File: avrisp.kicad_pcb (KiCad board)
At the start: 2 copper layers, 25 parts, among them J3 USB_A, J4 CONN_02X05, U1 ATMEGA8-16PU, Y1 12MHz

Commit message: last changes
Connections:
- net Net-(D3-Pad3) renamed /data+
- net Net-(D4-Pad3) renamed /data-
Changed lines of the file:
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@@
   (layers
     (0 F.Cu signal)
-    (31 B.Cu signal hide)
-    (32 B.Adhes user hide)
-    (33 F.Adhes user hide)
-    (34 B.Paste user hide)
-    (35 F.Paste user hide)
-    (36 B.SilkS user hide)
-    (37 F.SilkS user hide)
-    (38 B.Mask user hide)
-    (39 F.Mask user hide)
-    (40 Dwgs.User user hide)
-    (41 Cmts.User user hide)
-    (42 Eco1.User user hide)
-    (43 Eco2.User user hide)
-    (44 Edge.Cuts user hide)
-    (45 Margin user hide)
-    (46 B.CrtYd user hide)
-    (47 F.CrtYd user hide)
-    (48 B.Fab user hide)
-    (49 F.Fab user hide)
+    (31 B.Cu signal)
+    (32 B.Adhes user)
+    (33 F.Adhes user)
+    (34 B.Paste user)
+    (35 F.Paste user)
+    (36 B.SilkS user)
+    (37 F.SilkS user)
+    (38 B.Mask user)
+    (39 F.Mask user)
+    (40 Dwgs.User user)
+    (41 Cmts.User user)
+    (42 Eco1.User user)
+    (43 Eco2.User user)
+    (44 Edge.Cuts user)
+    (45 Margin user)
+    (46 B.CrtYd user)
+    (47 F.CrtYd user)
+    (48 B.Fab user)
+    (49 F.Fab user)
   )
   (setup
@@
   (net 32 "Net-(J4-Pad2)")
   (net 33 "Net-(J4-Pad3)")
-  (net 34 "Net-(D4-Pad3)")
-  (net 35 "Net-(D3-Pad3)")
+  (net 34 /data-)
+  (net 35 /data+)
   (net_class Default "This is the default net class."
     (clearance 0.7)
@@
     (diff_pair_width 0.2)
     (add_net +5V)
+    (add_net /data+)
+    (add_net /data-)
     (add_net GND)
     (add_net "Net-(C1-Pad1)")
@@
     (add_net "Net-(D2-Pad1)")
     (add_net "Net-(D2-Pad2)")
-    (add_net "Net-(D3-Pad3)")
-    (add_net "Net-(D4-Pad3)")
     (add_net "Net-(J4-Pad1)")
     (add_net "Net-(J4-Pad2)")
@@
       (net 7 +5V))
     (pad 2 thru_hole circle (at 2.54 0 180) (size 1.5 1.5) (drill 0.9) (layers *.Cu *.Mask)
-      (net 34 "Net-(D4-Pad3)"))
+      (net 34 /data-))
     (pad 3 thru_hole circle (at 4.57 0 180) (size 1.5 1.5) (drill 0.9) (layers *.Cu *.Mask)
-      (net 35 "Net-(D3-Pad3)"))
+      (net 35 /data+))
     (pad 4 thru_hole circle (at 7.11 0 180) (size 1.5 1.5) (drill 0.9) (layers *.Cu *.Mask)
       (net 1 GND))
@@
       (net 7 +5V))
     (pad 2 thru_hole oval (at 10.16 0 180) (size 1.6 1.6) (drill 0.8) (layers *.Cu *.Mask)
-      (net 34 "Net-(D4-Pad3)"))
+      (net 34 /data-))
     (model Resistors_THT.3dshapes/R_Axial_DIN0207_L6.3mm_D2.5mm_P10.16mm_Horizontal.wrl
       (at (xyz 0 0 0))
@@
     (fp_line (start 1.93 -1.25) (end 1.93 1.25) (layer F.Fab) (width 0.1))
     (pad 2 thru_hole oval (at 10.16 0 180) (size 1.6 1.6) (drill 0.8) (layers *.Cu *.Mask)
-      (net 34 "Net-(D4-Pad3)"))
+      (net 34 /data-))
     (pad 1 thru_hole circle (at 0 0 180) (size 1.6 1.6) (drill 0.8) (layers *.Cu *.Mask)
       (net 15 "Net-(R8-Pad1)"))
@@
     (fp_line (start 1.93 -1.25) (end 1.93 1.25) (layer F.Fab) (width 0.1))
     (pad 2 thru_hole oval (at 10.16 0) (size 1.6 1.6) (drill 0.8) (layers *.Cu *.Mask)
-      (net 35 "Net-(D3-Pad3)"))
+      (net 35 /data+))
     (pad 1 thru_hole circle (at 0 0) (size 2 2) (drill 0.8) (layers *.Cu *.Mask)
       (net 2 "Net-(R9-Pad1)"))
@@
     (pad 2 smd rect (at -1 0.95) (size 0.9 0.8) (layers F.Cu F.Paste F.Mask))
     (pad 3 smd rect (at 1 0) (size 0.9 0.8) (layers F.Cu F.Paste F.Mask)
-      (net 35 "Net-(D3-Pad3)"))
+      (net 35 /data+))
     (model ${KISYS3DMOD}/TO_SOT_Packages_SMD.3dshapes/SOT-23.wrl
       (at (xyz 0 0 0))
@@
     )
     (pad 3 smd rect (at 1 0) (size 0.9 0.8) (layers F.Cu F.Paste F.Mask)
-      (net 34 "Net-(D4-Pad3)"))
+      (net 34 /data-))
     (pad 2 smd rect (at -1 0.95) (size 0.9 0.8) (layers F.Cu F.Paste F.Mask))
     (pad 1 smd rect (at -1 -0.95) (size 0.9 0.8) (layers F.Cu F.Paste F.Mask)

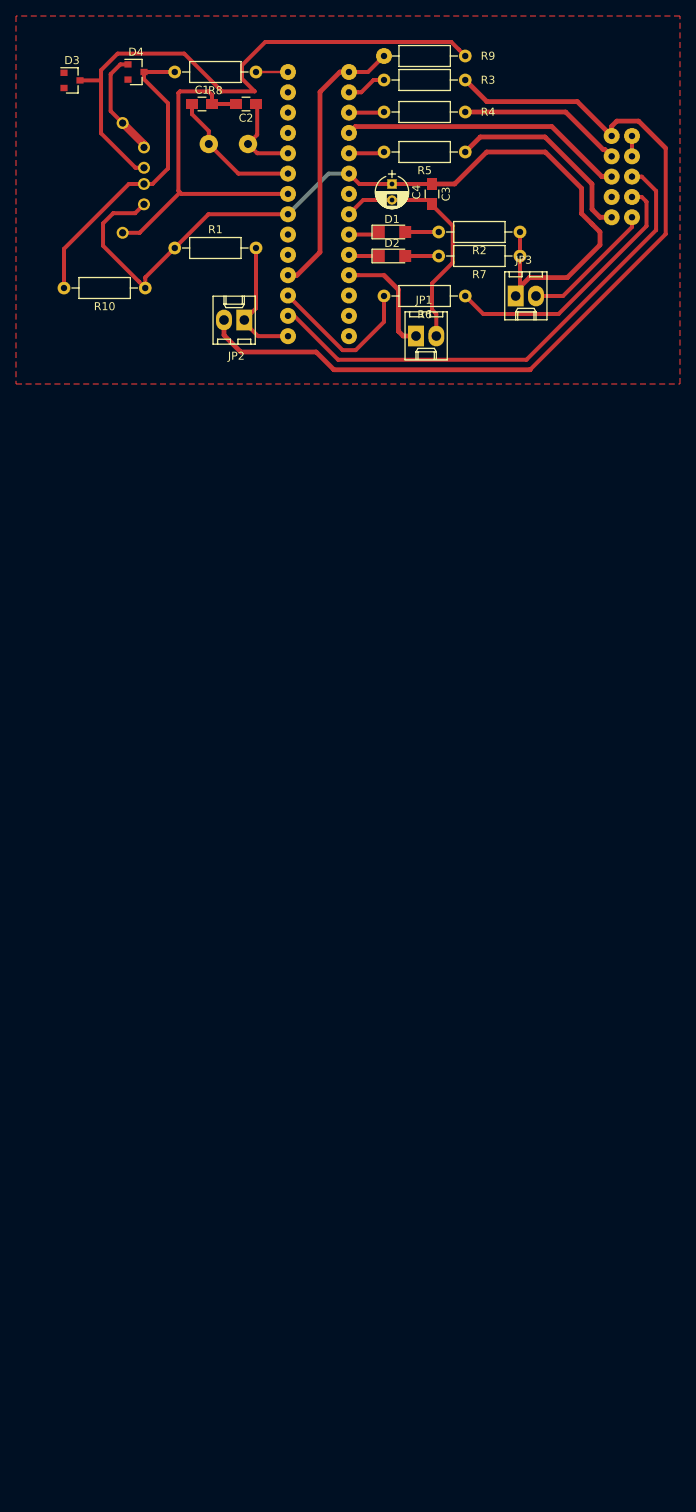
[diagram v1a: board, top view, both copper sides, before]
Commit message: Make one sided PCB but with smd components
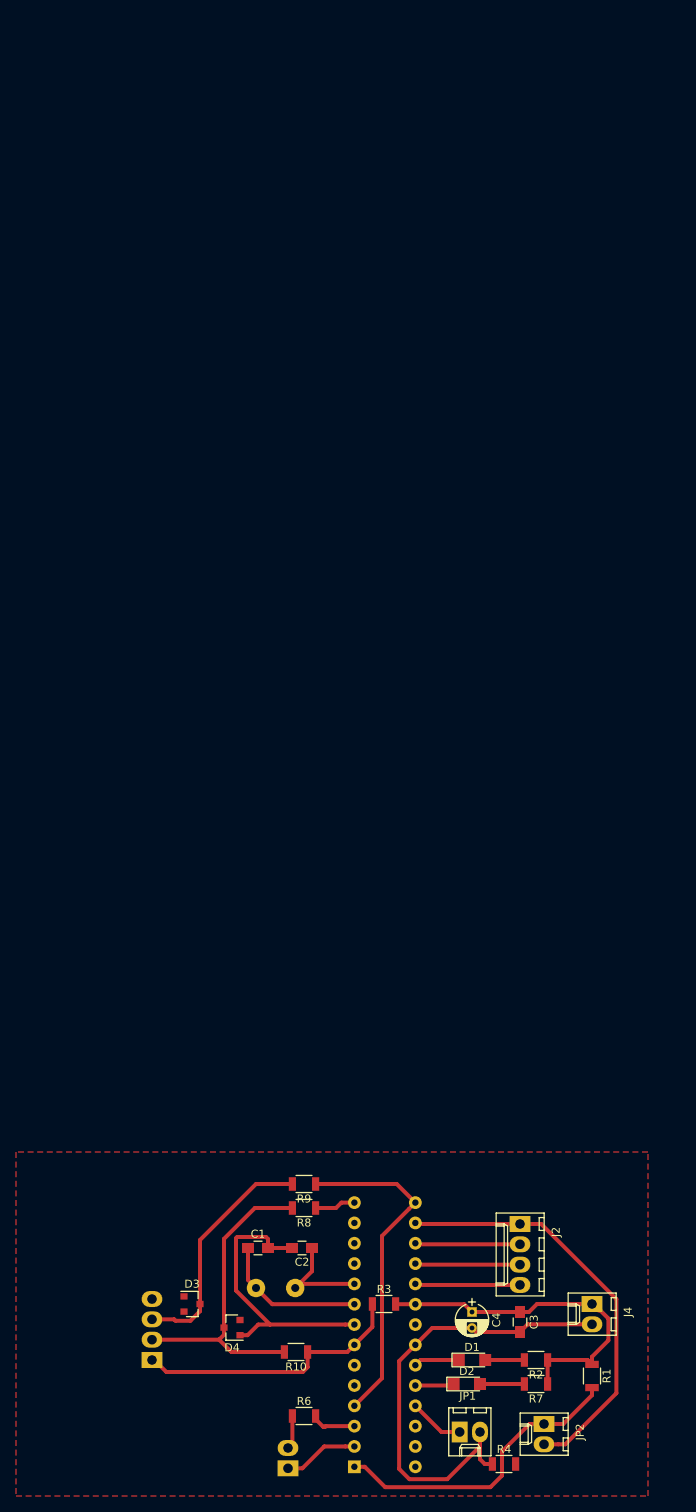
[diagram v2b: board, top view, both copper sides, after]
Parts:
- removed JP3: vtarget, Connectors_Molex:Molex_KK-6410-02_02x2.54mm_Straight
- removed R5: 270, Resistors_THT:R_Axial_DIN0207_L6.3mm_D2.5mm_P10.16mm_Horizontal
- added J1: serial1, Connectors_Molex:Molex_KK-6410-02_02x2.54mm_Straight, B.Cu at (46.0, 193.5)
- added J2: CONN_01X04, Connectors_Molex:Molex_KK-6410-04_04x2.54mm_Straight, F.Cu at (75.0, 163.0)
- J3: value USB_A -> CONN_01X04; footprint Connectors:USB_A -> Connectors_Molex:Molex_KK-6410-04_04x2.54mm_Straight
- J4: value CONN_02X05 -> power; footprint Connectors:IDC_Header_Straight_10pins -> Connectors_Molex:Molex_KK-6410-02_02x2.54mm_Straight; moved to F.Cu
- R1, R10, R2, R7, R8, R9: footprint Resistors_THT:R_Axial_DIN0207_L6.3mm_D2.5mm_P10.16mm_Horizontal -> Resistors_SMD:R_1206
- R3, R4: value 270 -> 0; footprint Resistors_THT:R_Axial_DIN0207_L6.3mm_D2.5mm_P10.16mm_Horizontal -> Resistors_SMD:R_1206
- R6: value 270 -> 1K; footprint Resistors_THT:R_Axial_DIN0207_L6.3mm_D2.5mm_P10.16mm_Horizontal -> Resistors_SMD:R_1206
- moved R4 169.1 mm to (73.0, 193.0), turned to 0 degrees
- moved D4 157.4 mm to (39.0, 175.9), turned to 180 degrees
- moved D3 153.7 mm to (34.0, 173.0)
- moved R3 153.3 mm to (58.0, 173.0), turned to 0 degrees
- moved R1 150.3 mm to (84.0, 182.0), turned to 270 degrees
- moved J3 144.5 mm to (29.0, 180.0)
- moved C1 143.2 mm to (42.2, 166.0)
- moved C2 143.2 mm to (47.8, 166.0)
- moved Y1 143.1 mm to (42.0, 171.0)
- moved JP2 143.0 mm to (78.0, 188.0), turned to 270 degrees
- moved R8 142.1 mm to (48.0, 161.0)
- moved U1 141.6 mm to (54.3, 193.3)
- moved R6 141.4 mm to (48.0, 187.0), turned to 0 degrees
- moved C3 141.4 mm to (75.0, 175.2)
- moved C4 141.4 mm to (69.0, 174.0)
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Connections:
- net Net-(JP2-Pad1) renamed /reset
- net Net-(R6-Pad2) renamed /tx
- J4 pad 1: Net-(J4-Pad1) -> +5V
- J4 pad 2: Net-(J4-Pad2) -> GND
- JP2 pad 2: Net-(J4-Pad9) -> /ss
- R3 pad 1: Net-(J4-Pad9) -> +5V
- R3 pad 2: Net-(R3-Pad2) -> +5V
- R4 pad 1: Net-(J4-Pad7) -> GND
- R4 pad 2: Net-(R4-Pad2) -> GND
- R6 pad 1: Net-(J4-Pad4) -> Net-(J1-Pad2)
- U1 pad 16: Net-(R3-Pad2) -> /ss
- U1 pad 17: Net-(R4-Pad2) -> /mosi
- U1 pad 18: Net-(J4-Pad5) -> /miso
- U1 pad 19: Net-(R5-Pad2) -> /sck
- U1 pad 2: Net-(J4-Pad6) -> /rx
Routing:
- net Net-(J4-Pad9): track 108.0 -> 0.00 mm
- net Net-(J4-Pad6): track 63.6 -> 0.00 mm
- net /ss: track 0.00 -> 52.5 mm
- net /data+: track 73.5 -> 29.9 mm
- net Net-(J4-Pad5): track 35.8 -> 0.00 mm
- net Net-(J4-Pad4): track 33.2 -> 0.00 mm
- net +5V: track 111.3 -> 78.2 mm
- net Net-(J4-Pad1): track 25.1 -> 0.00 mm
- net /reset: track 16.1 -> 38.5 mm
- net Net-(J4-Pad7): track 21.4 -> 0.00 mm
- net Net-(J4-Pad2): track 16.8 -> 0.00 mm
- net /tx: track 19.5 -> 5.68 mm
- net /miso: track 0.00 -> 13.1 mm
- net /sck: track 0.00 -> 13.1 mm
- net /mosi: track 0.00 -> 13.1 mm
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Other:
- net class 1 removed
- net class Default: clearance 0.7 -> 0.2; trace_width 0.6 -> 0.3; via_dia 1.5 -> 0.8; via_drill 0.5 -> 0.4
- net class thick added: clearance 0.5, trace_width 0.5, via_dia 1.2, via_drill 0.5
- rule pad_to_mask_clearance: 0.2 -> 0
- rule trace_clearance: 0.7 -> 0.2
- rule via_min_drill: 0.5 -> 0.3
- rule via_min_size: 0.5 -> 0.4
